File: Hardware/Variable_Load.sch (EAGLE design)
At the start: 51 parts, among them Q1 60V/32A/35mΩ, U1 CY8C5868LTI-LP039, U2 3.3V

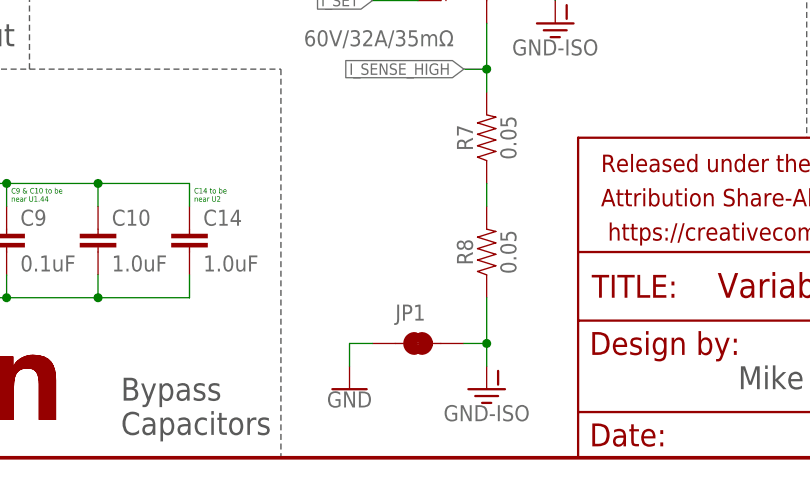
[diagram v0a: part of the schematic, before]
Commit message: Corrections from QC double check
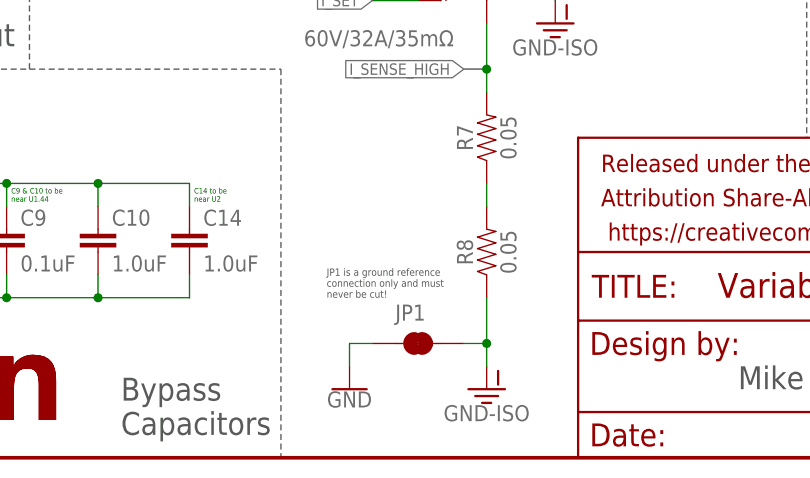
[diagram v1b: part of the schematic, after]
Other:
- note added: "JP1 is a ground reference connection only and must never be cut!"
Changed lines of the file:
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@@
 <text x="165.1" y="7.62" size="2.54" layer="97">Mike Hord</text>
 <text x="241.3" y="7.62" size="2.54" layer="97">01</text>
+<text x="119.38" y="17.78" size="0.8128" layer="97">JP1 is a ground reference
+connection only and must
+never be cut!</text>
 </plain>
 <instances>

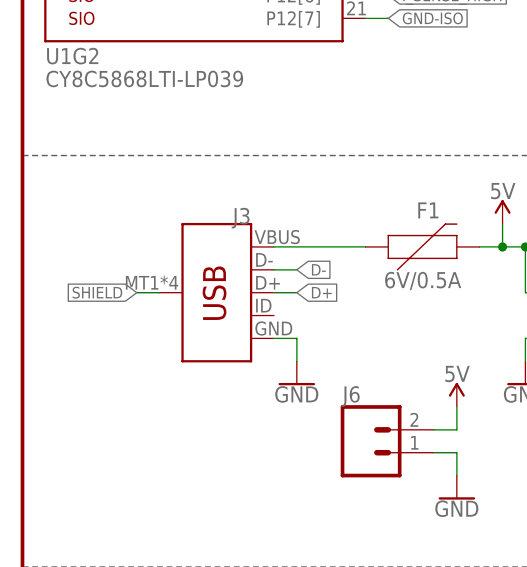
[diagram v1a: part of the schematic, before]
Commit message: Replace USB jack with newer, bossed design
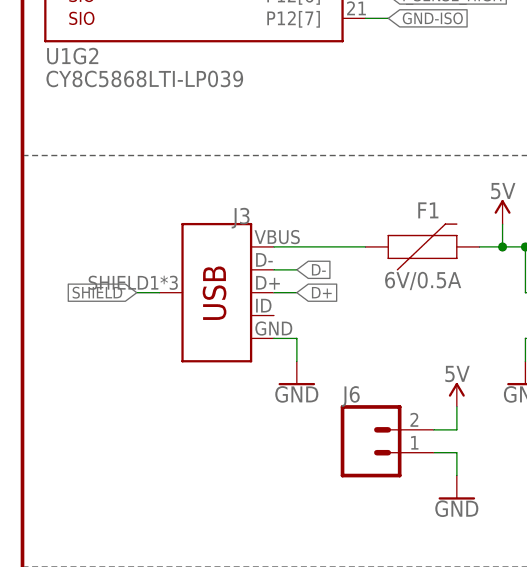
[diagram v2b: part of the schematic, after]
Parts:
- J3: device SparkFun-Connectors:USB_MICRO-B_SMT -> SparkFun-Connectors:USB_MICRO-B_FEMALE-SMT
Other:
- moved on the sheet: J3
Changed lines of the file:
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@@
 <?xml version="1.0" encoding="utf-8"?>
 <!DOCTYPE eagle SYSTEM "eagle.dtd">
-<eagle version="7.6.0">
+<eagle version="7.7.0">
 <drawing>
 <settings>
@@
 <part name="SUPPLY10" library="SparkFun-PowerSymbols" deviceset="5V" device=""/>
 <part name="U2" library="SparkFun-IC-Power" deviceset="V_REG_AP2112" device="K-3.3V" value="3.3V"/>
-<part name="J3" library="SparkFun-Connectors" deviceset="USB_MICRO-B" device="_SMT"/>
+<part name="J3" library="SparkFun-Connectors" deviceset="USB_MICRO-B" device="_FEMALE-SMT"/>
 <part name="SUPPLY11" library="SparkFun-PowerSymbols" deviceset="5V" device=""/>
 <part name="F1" library="SparkFun-Fuses" deviceset="PPTC" device="_HALF-AMP" value="6V/0.5A"/>

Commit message: Add firmware, latest changes to HW
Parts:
- added D1: GREEN, SparkFun-LED:LED1206-BOTTOM
- added R12: 560, SparkFun-Resistors:560OHM_0402_1%
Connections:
- new net N$12: D1.A, U1G4.P3[0]
- new net N$13: D1.C, R12.1
- net GND: now also R12.2
- net GND-ISO: now also U1G2.P1[7]; no longer U1G2.P12[7]
- net I_SENSE_HIGH: now also U1G2.P1[6]; no longer U1G2.P12[6]
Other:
- moved on the sheet: J5
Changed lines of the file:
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@@
 <part name="LOGO2" library="SparkFun-Aesthetics" deviceset="SFE_LOGO_NAME" device=".3_INCH" value="SFE_LOGO_NAME.3_INCH"/>
 <part name="LOGO3" library="SparkFun-Aesthetics" deviceset="SFE_LOGO_NAME" device=".3_INCH" value="SFE_LOGO_NAME.3_INCH"/>
+<part name="D1" library="SparkFun-LED" deviceset="LED" device="1206-BOTTOM" value="GREEN">
+<attribute name="PROD_ID" value="DIO-11076"/>
+</part>
+<part name="R12" library="SparkFun-Resistors" deviceset="560OHM" device="_0402_1%" value="560"/>
+<part name="GND5" library="SparkFun-PowerSymbols" deviceset="GND" device=""/>
 </parts>
 <sheets>
@@
 <instance part="H5" gate="G$1" x="246.38" y="33.02"/>
 <instance part="SUPPLY1" gate="G$1" x="33.02" y="35.56"/>
-<instance part="J5" gate="G$1" x="55.88" y="119.38"/>
-<instance part="SUPPLY7" gate="G$1" x="66.04" y="127"/>
-<instance part="GND11" gate="1" x="66.04" y="109.22"/>
+<instance part="J5" gate="G$1" x="60.96" y="137.16"/>
+<instance part="SUPPLY7" gate="G$1" x="71.12" y="144.78"/>
+<instance part="GND11" gate="1" x="71.12" y="127"/>
 <instance part="C13" gate="G$1" x="43.18" y="22.86"/>
 <instance part="C14" gate="G$1" x="104.14" y="22.86"/>
@@
 <instance part="LOGO2" gate="G$1" x="33.02" y="0"/>
 <instance part="LOGO3" gate="G$1" x="33.02" y="0"/>
+<instance part="D1" gate="G$1" x="137.16" y="121.92" rot="R90">
+<attribute name="PROD_ID" x="137.16" y="121.92" size="1.778" layer="96" rot="R90" display="off"/>
+</instance>
+<instance part="R12" gate="G$1" x="152.4" y="121.92" smashed="yes">
+<attribute name="NAME" x="156.972" y="122.174" size="1.778" layer="95" font="vector" align="bottom-center"/>
+<attribute name="VALUE" x="157.734" y="121.666" size="1.778" layer="96" font="vector" align="top-center"/>
+</instance>
+<instance part="GND5" gate="1" x="162.56" y="116.84"/>
 </instances>
 <busses>
@@
 <segment>
 <pinref part="J5" gate="G$1" pin="4"/>
-<wire x1="63.5" y1="121.92" x2="66.04" y2="121.92" width="0.1524" layer="91"/>
-<wire x1="66.04" y1="121.92" x2="66.04" y2="111.76" width="0.1524" layer="91"/>
+<wire x1="68.58" y1="139.7" x2="71.12" y2="139.7" width="0.1524" layer="91"/>
+<wire x1="71.12" y1="139.7" x2="71.12" y2="129.54" width="0.1524" layer="91"/>
 <pinref part="GND11" gate="1" pin="GND"/>
 </segment>
@@
 <pinref part="J7" gate="G$1" pin="4"/>
 <wire x1="182.88" y1="73.66" x2="185.42" y2="73.66" width="0.1524" layer="91"/>
+</segment>
+<segment>
+<pinref part="R12" gate="G$1" pin="2"/>
+<pinref part="GND5" gate="1" pin="GND"/>
+<wire x1="157.48" y1="121.92" x2="162.56" y2="121.92" width="0.1524" layer="91"/>
+<wire x1="162.56" y1="121.92" x2="162.56" y2="119.38" width="0.1524" layer="91"/>
 </segment>
 </net>
@@
 <segment>
 <pinref part="J5" gate="G$1" pin="5"/>
-<wire x1="63.5" y1="124.46" x2="66.04" y2="124.46" width="0.1524" layer="91"/>
-<wire x1="66.04" y1="124.46" x2="66.04" y2="127" width="0.1524" layer="91"/>
+<wire x1="68.58" y1="142.24" x2="71.12" y2="142.24" width="0.1524" layer="91"/>
+<wire x1="71.12" y1="142.24" x2="71.12" y2="144.78" width="0.1524" layer="91"/>
 <pinref part="SUPPLY7" gate="G$1" pin="5V"/>
 </segment>
@@
 </segment>
 <segment>
-<pinref part="U1" gate="G2" pin="P12[6]"/>
-<wire x1="38.1" y1="106.68" x2="40.64" y2="106.68" width="0.1524" layer="91"/>
-<label x="40.64" y="106.68" size="1.27" layer="95" xref="yes"/>
+<label x="40.64" y="111.76" size="1.27" layer="95" xref="yes"/>
+<pinref part="U1" gate="G2" pin="P1[6]"/>
+<wire x1="40.64" y1="111.76" x2="38.1" y2="111.76" width="0.1524" layer="91"/>
 </segment>
 </net>
@@
 </segment>
 <segment>
-<pinref part="U1" gate="G2" pin="P12[7]"/>
-<wire x1="38.1" y1="104.14" x2="40.64" y2="104.14" width="0.1524" layer="91"/>
-<label x="40.64" y="104.14" size="1.27" layer="95" xref="yes"/>
+<label x="40.64" y="109.22" size="1.27" layer="95" xref="yes"/>
+<pinref part="U1" gate="G2" pin="P1[7]"/>
+<wire x1="40.64" y1="109.22" x2="38.1" y2="109.22" width="0.1524" layer="91"/>
 </segment>
 </net>
@@
 <segment>
 <pinref part="J5" gate="G$1" pin="3"/>
-<wire x1="63.5" y1="119.38" x2="68.58" y2="119.38" width="0.1524" layer="91"/>
-<label x="68.58" y="119.38" size="1.27" layer="95" xref="yes"/>
+<wire x1="68.58" y1="137.16" x2="73.66" y2="137.16" width="0.1524" layer="91"/>
+<label x="73.66" y="137.16" size="1.27" layer="95" xref="yes"/>
 </segment>
 <segment>
@@
 <segment>
 <pinref part="J5" gate="G$1" pin="2"/>
-<wire x1="63.5" y1="116.84" x2="68.58" y2="116.84" width="0.1524" layer="91"/>
-<label x="68.58" y="116.84" size="1.27" layer="95" xref="yes"/>
+<wire x1="68.58" y1="134.62" x2="73.66" y2="134.62" width="0.1524" layer="91"/>
+<label x="73.66" y="134.62" size="1.27" layer="95" xref="yes"/>
 </segment>
 <segment>
@@
 <segment>
 <pinref part="J5" gate="G$1" pin="1"/>
-<wire x1="63.5" y1="114.3" x2="68.58" y2="114.3" width="0.1524" layer="91"/>
-<label x="68.58" y="114.3" size="1.27" layer="95" xref="yes"/>
+<wire x1="68.58" y1="132.08" x2="73.66" y2="132.08" width="0.1524" layer="91"/>
+<label x="73.66" y="132.08" size="1.27" layer="95" xref="yes"/>
 </segment>
 <segment>
@@
 </segment>
 </net>
+<net name="N$12" class="0">
+<segment>
+<pinref part="U1" gate="G4" pin="P3[0]"/>
+<wire x1="129.54" y1="121.92" x2="134.62" y2="121.92" width="0.1524" layer="91"/>
+<pinref part="D1" gate="G$1" pin="A"/>
+</segment>
+</net>
+<net name="N$13" class="0">
+<segment>
+<pinref part="D1" gate="G$1" pin="C"/>
+<pinref part="R12" gate="G$1" pin="1"/>
+<wire x1="147.32" y1="121.92" x2="142.24" y2="121.92" width="0.1524" layer="91"/>
+</segment>
+</net>

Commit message: Changes from design review
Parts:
- J3: value (none) -> AMP FCI 10103594-0001LF; device SparkFun-Connectors:USB_MICRO-B_FEMALE-SMT -> SparkFun-Connectors:USB_MICRO-B_HALF_PTH
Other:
- note added: "10"
- note removed: "01"
- moved on the sheet: J3
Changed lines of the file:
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@@
 <part name="SUPPLY10" library="SparkFun-PowerSymbols" deviceset="5V" device=""/>
 <part name="U2" library="SparkFun-IC-Power" deviceset="V_REG_AP2112" device="K-3.3V" value="3.3V"/>
-<part name="J3" library="SparkFun-Connectors" deviceset="USB_MICRO-B" device="_FEMALE-SMT"/>
+<part name="J3" library="SparkFun-Connectors" deviceset="USB_MICRO-B" device="_HALF_PTH" value="AMP FCI 10103594-0001LF"/>
 <part name="SUPPLY11" library="SparkFun-PowerSymbols" deviceset="5V" device=""/>
 <part name="F1" library="SparkFun-Fuses" deviceset="PPTC" device="_HALF-AMP" value="6V/0.5A"/>
@@
 Capacitors</text>
 <text x="165.1" y="7.62" size="2.54" layer="97">Mike Hord</text>
-<text x="241.3" y="7.62" size="2.54" layer="97">01</text>
+<text x="241.3" y="7.62" size="2.54" layer="97">10</text>
 <text x="119.38" y="17.78" size="0.8128" layer="97">JP1 is a ground reference
 connection only and must
@@
 <instance part="SUPPLY10" gate="G$1" x="208.28" y="99.06"/>
 <instance part="U2" gate="G$1" x="68.58" y="73.66"/>
-<instance part="J3" gate="G$1" x="22.86" y="73.66" rot="MR0"/>
+<instance part="J3" gate="G$1" x="22.86" y="73.66" smashed="yes" rot="MR0">
+<attribute name="NAME" x="25.4" y="81.28" size="1.778" layer="95" font="vector" rot="MR0"/>
+</instance>
 <instance part="SUPPLY11" gate="G$1" x="53.34" y="81.28"/>
 <instance part="F1" gate="G$1" x="43.18" y="78.74"/>
@@
 <segment>
 <pinref part="J3" gate="G$1" pin="SHIELD"/>
-<wire x1="15.24" y1="73.66" x2="12.7" y2="73.66" width="0.1524" layer="91"/>
-<label x="12.7" y="73.66" size="1.27" layer="95" rot="R180" xref="yes"/>
-</segment>
-</net>
+<wire x1="15.24" y1="73.66" x2="10.16" y2="73.66" width="0.1524" layer="91"/>
+<label x="10.16" y="73.66" size="1.27" layer="95" rot="R180" xref="yes"/>
+</segment>
+</net>

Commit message: Changes for 2nd proto round
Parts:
- added R13: 1k, SparkFun-Resistors:1KOHM-0603-1/10W-1%
- added R14: 4.7k, SparkFun-Resistors:4.7KOHM-0603-1/10W-1%
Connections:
- new net CONTRAST: J2.3, R13.2, R14.1
- net 5V: now also R14.2
- net GND: now also R13.1; no longer J2.3
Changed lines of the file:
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@@
 <part name="R12" library="SparkFun-Resistors" deviceset="560OHM" device="_0402_1%" value="560"/>
 <part name="GND5" library="SparkFun-PowerSymbols" deviceset="GND" device=""/>
+<part name="R13" library="SparkFun-Resistors" deviceset="1KOHM" device="-0603-1/10W-1%" value="1k"/>
+<part name="R14" library="SparkFun-Resistors" deviceset="4.7KOHM" device="-0603-1/10W-1%" value="4.7k"/>
+<part name="GND14" library="SparkFun-PowerSymbols" deviceset="GND" device=""/>
+<part name="SUPPLY9" library="SparkFun-PowerSymbols" deviceset="5V" device=""/>
 </parts>
 <sheets>
@@
 <instance part="GND3" gate="1" x="182.88" y="116.84"/>
 <instance part="J2" gate="G$1" x="223.52" y="76.2" rot="R180"/>
-<instance part="GND6" gate="1" x="198.12" y="91.44"/>
+<instance part="GND6" gate="1" x="190.5" y="91.44"/>
 <instance part="SUPPLY10" gate="G$1" x="208.28" y="99.06"/>
 <instance part="U2" gate="G$1" x="68.58" y="73.66"/>
@@
 </instance>
 <instance part="GND5" gate="1" x="162.56" y="116.84"/>
+<instance part="R13" gate="G$1" x="243.84" y="71.12" rot="R90"/>
+<instance part="R14" gate="G$1" x="243.84" y="86.36" rot="R90"/>
+<instance part="GND14" gate="1" x="243.84" y="60.96"/>
+<instance part="SUPPLY9" gate="G$1" x="243.84" y="93.98"/>
 </instances>
 <busses>
@@
 <segment>
 <pinref part="GND6" gate="1" pin="GND"/>
-<wire x1="198.12" y1="93.98" x2="198.12" y2="96.52" width="0.1524" layer="91"/>
+<wire x1="190.5" y1="93.98" x2="190.5" y2="96.52" width="0.1524" layer="91"/>
 <pinref part="J2" gate="G$1" pin="1"/>
-<wire x1="198.12" y1="96.52" x2="210.82" y2="96.52" width="0.1524" layer="91"/>
-<wire x1="210.82" y1="96.52" x2="213.36" y2="96.52" width="0.1524" layer="91"/>
-<wire x1="210.82" y1="96.52" x2="210.82" y2="91.44" width="0.1524" layer="91"/>
-<junction x="210.82" y="96.52"/>
-<pinref part="J2" gate="G$1" pin="3"/>
-<wire x1="210.82" y1="91.44" x2="213.36" y2="91.44" width="0.1524" layer="91"/>
+<wire x1="190.5" y1="96.52" x2="213.36" y2="96.52" width="0.1524" layer="91"/>
 </segment>
 <segment>
@@
 <wire x1="157.48" y1="121.92" x2="162.56" y2="121.92" width="0.1524" layer="91"/>
 <wire x1="162.56" y1="121.92" x2="162.56" y2="119.38" width="0.1524" layer="91"/>
+</segment>
+<segment>
+<pinref part="R13" gate="G$1" pin="1"/>
+<pinref part="GND14" gate="1" pin="GND"/>
+<wire x1="243.84" y1="66.04" x2="243.84" y2="63.5" width="0.1524" layer="91"/>
 </segment>
 </net>
@@
 <wire x1="182.88" y1="76.2" x2="182.88" y2="83.82" width="0.1524" layer="91"/>
 </segment>
+<segment>
+<pinref part="SUPPLY9" gate="G$1" pin="5V"/>
+<pinref part="R14" gate="G$1" pin="2"/>
+<wire x1="243.84" y1="93.98" x2="243.84" y2="91.44" width="0.1524" layer="91"/>
+</segment>
 </net>
 <net name="N$10" class="0">
@@
 </segment>
 </net>
+<net name="CONTRAST" class="0">
+<segment>
+<pinref part="J2" gate="G$1" pin="3"/>
+<wire x1="210.82" y1="91.44" x2="213.36" y2="91.44" width="0.1524" layer="91"/>
+<label x="210.82" y="91.44" size="1.27" layer="95" rot="R180" xref="yes"/>
+</segment>
+<segment>
+<pinref part="R13" gate="G$1" pin="2"/>
+<pinref part="R14" gate="G$1" pin="1"/>
+<wire x1="243.84" y1="76.2" x2="243.84" y2="78.74" width="0.1524" layer="91"/>
+<wire x1="243.84" y1="78.74" x2="243.84" y2="81.28" width="0.1524" layer="91"/>
+<wire x1="243.84" y1="78.74" x2="241.3" y2="78.74" width="0.1524" layer="91"/>
+<junction x="243.84" y="78.74"/>
+<label x="241.3" y="78.74" size="1.27" layer="95" rot="R180" xref="yes"/>
+</segment>
+</net>

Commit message: Added resistor divider for contrast
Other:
- note added: "11"
- note removed: "10"
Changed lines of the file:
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@@
 Capacitors</text>
 <text x="165.1" y="7.62" size="2.54" layer="97">Mike Hord</text>
-<text x="241.3" y="7.62" size="2.54" layer="97">10</text>
+<text x="241.3" y="7.62" size="2.54" layer="97">11</text>
 <text x="119.38" y="17.78" size="0.8128" layer="97">JP1 is a ground reference
 connection only and must
